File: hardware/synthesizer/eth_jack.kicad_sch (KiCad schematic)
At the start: 4 parts, among them J11 RJ45_Abracon_ARJP11A-MASA-B-A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

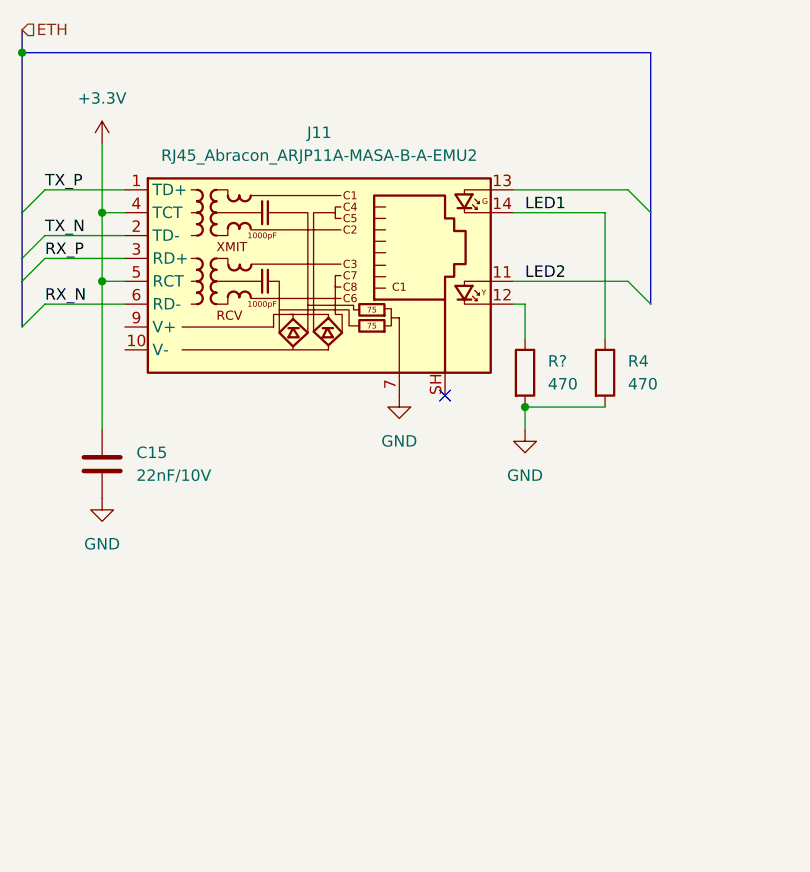
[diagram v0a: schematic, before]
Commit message: finish ethernet jack
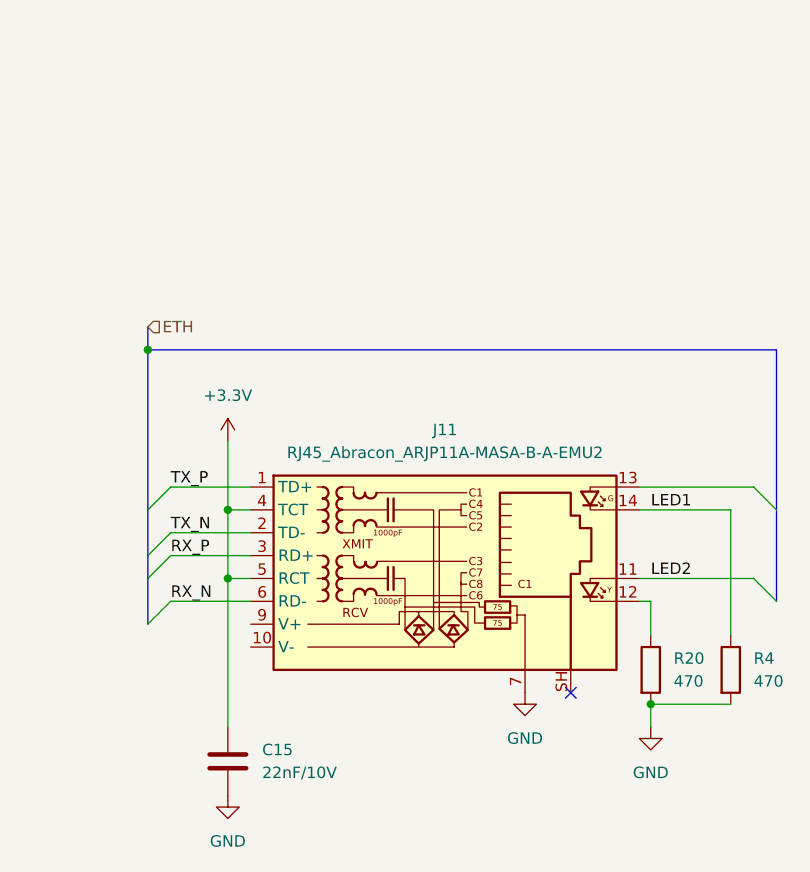
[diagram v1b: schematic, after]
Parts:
- gave numbers to parts that had none: 1
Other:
- moved on the sheet: C15, J11, R20, R4

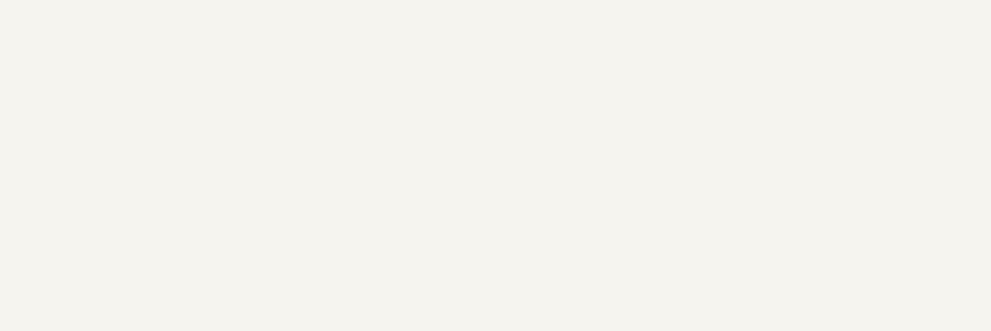
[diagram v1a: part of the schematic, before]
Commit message: add logo to every sheet
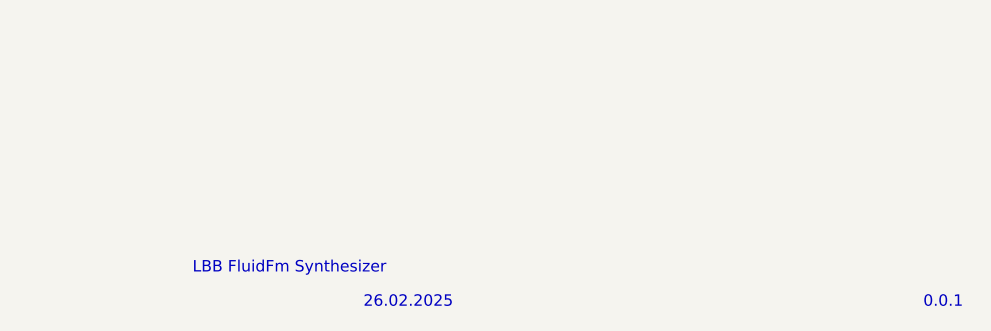
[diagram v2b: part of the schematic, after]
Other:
- note added: "0.0.1"
- note added: "26.02.2025"
- note added: "LBB FluidFm Synthesizer"

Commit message: improved pcb design
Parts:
- R20, R4: footprint (none) -> Resistor_SMD:R_0603_1608Metric
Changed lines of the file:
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@@
 			)
 		)
-		(property "Footprint" ""
+		(property "Footprint" "Resistor_SMD:R_0603_1608Metric"
 			(at 146.812 109.22 90)
 			(effects
@@
 			)
 		)
-		(property "Footprint" ""
+		(property "Footprint" "Resistor_SMD:R_0603_1608Metric"
 			(at 155.702 109.22 90)
 			(effects
